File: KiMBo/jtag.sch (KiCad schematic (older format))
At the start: 9 parts, among them U2 OSD3358, Y2 32.768kHz, Y3 24MHz

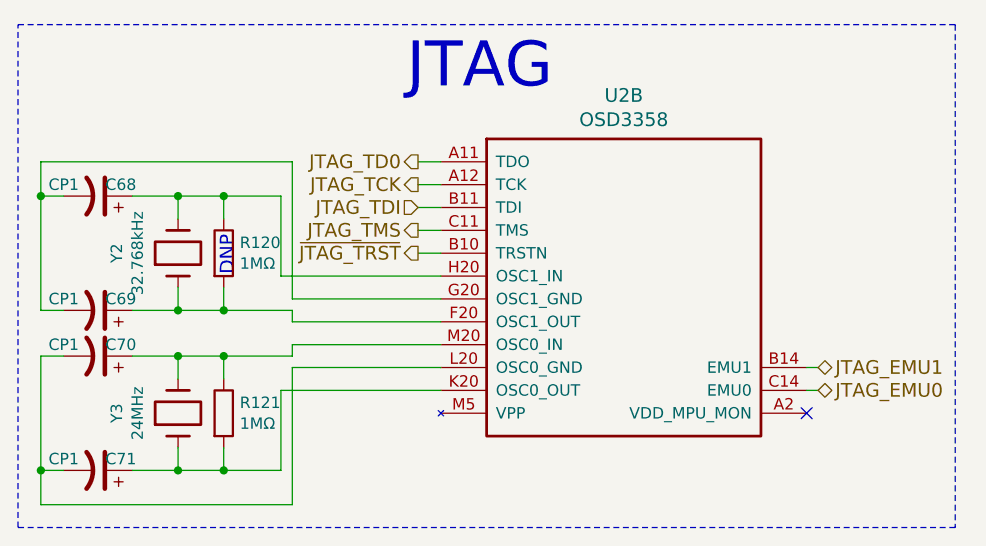
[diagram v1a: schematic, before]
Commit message: Entry of additional component values
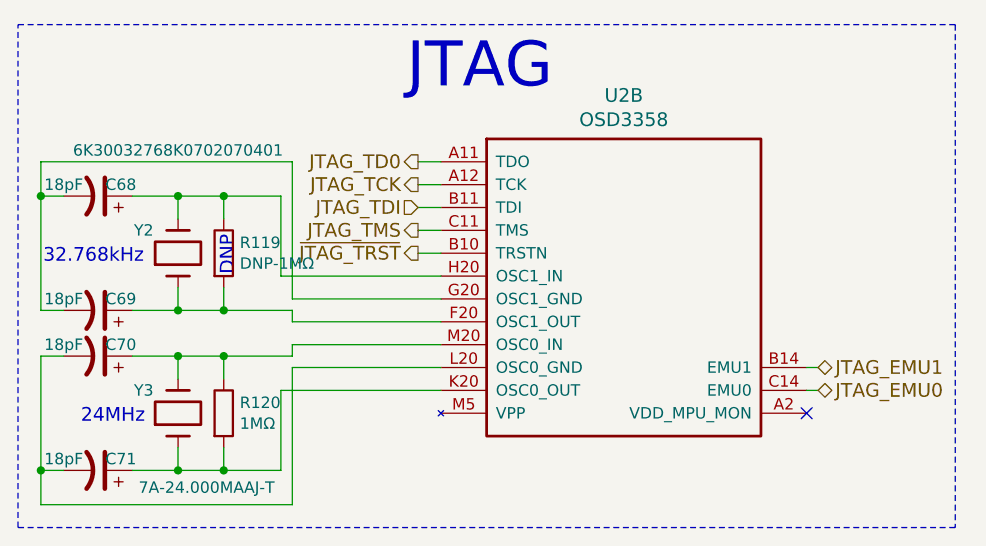
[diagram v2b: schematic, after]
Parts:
- C68, C69, C70, C71: value CP1 -> 18pF
- R119: renamed from R120; value 1MΩ -> DNP-1MΩ
- Y2: value 32.768kHz -> 6K30032768K0702070401
- Y3: value 24MHz -> 7A-24.000MAAJ-T
- renumbered R121 to R120
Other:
- note added: "24MHz"
- note added: "32.768kHz"
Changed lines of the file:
@@
 JTAG
 $Comp
-L R R121
+L R R120
 U 1 1 589C1CFA
 P 4900 4000
-F 0 "R121" H 4970 4046 50  0000 L CNN
+F 0 "R120" H 4970 4046 50  0000 L CNN
 F 1 "1MΩ" H 4970 3955 50  0000 L CNN
 F 2 "" V 4830 4000 50  0001 C CNN
@@
 P 4350 3750
 F 0 "C70" V 4400 3850 50  0000 C CNN
-F 1 "CP1" V 4400 3600 50  0000 C CNN
+F 1 "18pF" V 4400 3600 50  0000 C CNN
 F 2 "" H 4350 3750 50  0001 C CNN
 F 3 "" H 4350 3750 50  0000 C CNN
@@
 P 4350 4250
 F 0 "C71" V 4400 4350 50  0000 C CNN
-F 1 "CP1" V 4400 4100 50  0000 C CNN
+F 1 "18pF" V 4400 4100 50  0000 C CNN
 F 2 "" H 4350 4250 50  0001 C CNN
 F 3 "" H 4350 4250 50  0000 C CNN
@@
 $EndComp
 $Comp
-L R R120
+L R R119
 U 1 1 589C1D0F
 P 4900 3300
-F 0 "R120" H 4970 3346 50  0000 L CNN
-F 1 "1MΩ" H 4970 3255 50  0000 L CNN
+F 0 "R119" H 4970 3346 50  0000 L CNN
+F 1 "DNP-1MΩ" H 4970 3255 50  0000 L CNN
 F 2 "" V 4830 3300 50  0001 C CNN
 F 3 "" H 4900 3300 50  0000 C CNN
@@
 P 4350 3550
 F 0 "C69" V 4400 3650 50  0000 C CNN
-F 1 "CP1" V 4400 3400 50  0000 C CNN
+F 1 "18pF" V 4400 3400 50  0000 C CNN
 F 2 "" H 4350 3550 50  0001 C CNN
 F 3 "" H 4350 3550 50  0000 C CNN
@@
 P 4350 3050
 F 0 "C68" V 4400 3150 50  0000 C CNN
-F 1 "CP1" V 4400 2900 50  0000 C CNN
+F 1 "18pF" V 4400 2900 50  0000 C CNN
 F 2 "" H 4350 3050 50  0001 C CNN
 F 3 "" H 4350 3050 50  0000 C CNN
@@
 U 1 1 589C1D2C
 P 4700 4000
-F 0 "Y3" H 4700 4268 50  0000 C CNN
-F 1 "24MHz" H 4700 4177 50  0000 C CNN
+F 0 "Y3" V 4800 4150 50  0000 C CNN
+F 1 "7A-24.000MAAJ-T" V 4375 3875 50  0000 C CNN
 F 2 "" H 4700 4000 50  0001 C CNN
 F 3 "" H 4700 4000 50  0000 C CNN
@@
 U 1 1 589C1D33
 P 4700 3300
-F 0 "Y2" H 4700 3568 50  0000 C CNN
-F 1 "32.768kHz" H 4700 3477 50  0000 C CNN
+F 0 "Y2" V 4800 3450 50  0000 C CNN
+F 1 "6K30032768K0702070401" V 5150 3300 50  0000 C CNN
 F 2 "" H 4700 3300 50  0001 C CNN
 F 3 "" H 4700 3300 50  0000 C CNN
@@
 Text Notes 4950 3400 1    60   ~ 0
 DNP
+Text Notes 4110 3350 0    60   ~ 0
+32.768kHz
+Text Notes 4275 4050 0    60   ~ 0
+24MHz
 $EndSCHEMATC

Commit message: Replace most electrolytic cap symbols symbols with the standard, non-polarized (ceramic) cap symbol
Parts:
- C68, C69, C70, C71: symbol CP1 -> C
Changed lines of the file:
@@
 $EndComp
 $Comp
-L CP1 C70
+L C C70
 U 1 1 589C1D01
 P 4350 3750
@@
 $EndComp
 $Comp
-L CP1 C71
+L C C71
 U 1 1 589C1D08
 P 4350 4250
@@
 $EndComp
 $Comp
-L CP1 C69
+L C C69
 U 1 1 589C1D16
 P 4350 3550
@@
 $EndComp
 $Comp
-L CP1 C68
+L C C68
 U 1 1 589C1D1D
 P 4350 3050

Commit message: Add equivalent annotations document, associate more footprints
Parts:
- C68, C69, C70, C71: footprint (none) -> Capacitors_SMD:C_0402
- R118: renamed from R119; footprint (none) -> Resistors_SMD:R_0402
- R119: renamed from R120; footprint (none) -> Resistors_SMD:R_0402
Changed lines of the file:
@@
 JTAG
 $Comp
-L R R120
+L R R119
 U 1 1 589C1CFA
 P 4900 4000
-F 0 "R120" H 4970 4046 50  0000 L CNN
+F 0 "R119" H 4970 4046 50  0000 L CNN
 F 1 "1MΩ" H 4970 3955 50  0000 L CNN
-F 2 "" V 4830 4000 50  0001 C CNN
+F 2 "Resistors_SMD:R_0402" V 4830 4000 50  0001 C CNN
 F 3 "" H 4900 4000 50  0000 C CNN
 	1    4900 4000
@@
 F 0 "C70" V 4400 3850 50  0000 C CNN
 F 1 "18pF" V 4400 3600 50  0000 C CNN
-F 2 "" H 4350 3750 50  0001 C CNN
+F 2 "Capacitors_SMD:C_0402" H 4350 3750 50  0001 C CNN
 F 3 "" H 4350 3750 50  0000 C CNN
 	1    4350 3750
@@
 F 0 "C71" V 4400 4350 50  0000 C CNN
 F 1 "18pF" V 4400 4100 50  0000 C CNN
-F 2 "" H 4350 4250 50  0001 C CNN
+F 2 "Capacitors_SMD:C_0402" H 4350 4250 50  0001 C CNN
 F 3 "" H 4350 4250 50  0000 C CNN
 	1    4350 4250
@@
 $EndComp
 $Comp
-L R R119
+L R R118
 U 1 1 589C1D0F
 P 4900 3300
-F 0 "R119" H 4970 3346 50  0000 L CNN
+F 0 "R118" H 4970 3346 50  0000 L CNN
 F 1 "DNP-1MΩ" H 4970 3255 50  0000 L CNN
-F 2 "" V 4830 3300 50  0001 C CNN
+F 2 "Resistors_SMD:R_0402" V 4830 3300 50  0001 C CNN
 F 3 "" H 4900 3300 50  0000 C CNN
 	1    4900 3300
@@
 F 0 "C69" V 4400 3650 50  0000 C CNN
 F 1 "18pF" V 4400 3400 50  0000 C CNN
-F 2 "" H 4350 3550 50  0001 C CNN
+F 2 "Capacitors_SMD:C_0402" H 4350 3550 50  0001 C CNN
 F 3 "" H 4350 3550 50  0000 C CNN
 	1    4350 3550
@@
 F 0 "C68" V 4400 3150 50  0000 C CNN
 F 1 "18pF" V 4400 2900 50  0000 C CNN
-F 2 "" H 4350 3050 50  0001 C CNN
+F 2 "Capacitors_SMD:C_0402" H 4350 3050 50  0001 C CNN
 F 3 "" H 4350 3050 50  0000 C CNN
 	1    4350 3050

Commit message: Leave SPI0 free for a display, reassign pins so SPI1 is available
Fix some typos/errors
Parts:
- renumbered R118 to R120, R119 to R121, U2 to U1
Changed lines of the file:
@@
 P 5850 2900
 AR Path="/581AEC7B/589C1CF2" Ref="U?"  Part="2"
-AR Path="/589C1616/589C1CF2" Ref="U2"  Part="2"
-F 0 "U2" H 6650 3190 60  0000 C CNN
+AR Path="/589C1616/589C1CF2" Ref="U1"  Part="2"
+F 0 "U1" H 6650 3190 60  0000 C CNN
 F 1 "OSD3358" H 6650 3084 60  0000 C CNN
 F 2 "" H 5850 2900 60  0001 C CNN
@@
 JTAG
 $Comp
-L R R119
+L R R121
 U 1 1 589C1CFA
 P 4900 4000
-F 0 "R119" H 4970 4046 50  0000 L CNN
+F 0 "R121" H 4970 4046 50  0000 L CNN
 F 1 "1MΩ" H 4970 3955 50  0000 L CNN
 F 2 "Resistors_SMD:R_0402" V 4830 4000 50  0001 C CNN
@@
 $EndComp
 $Comp
-L R R118
+L R R120
 U 1 1 589C1D0F
 P 4900 3300
-F 0 "R118" H 4970 3346 50  0000 L CNN
+F 0 "R120" H 4970 3346 50  0000 L CNN
 F 1 "DNP-1MΩ" H 4970 3255 50  0000 L CNN
 F 2 "Resistors_SMD:R_0402" V 4830 3300 50  0001 C CNN

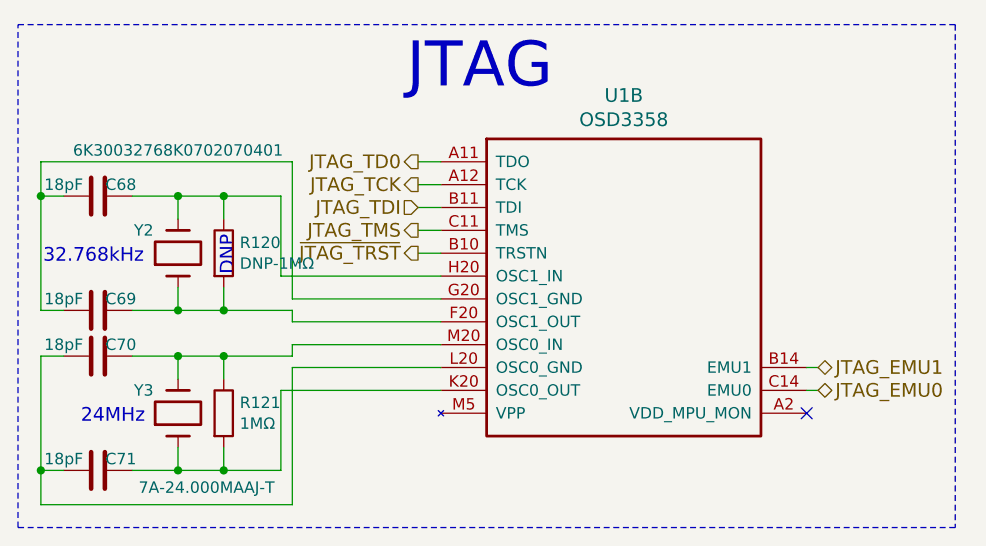
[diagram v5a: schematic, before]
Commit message: Use fixed 5V LM2592HV Buck, include SPI0 header for LCD
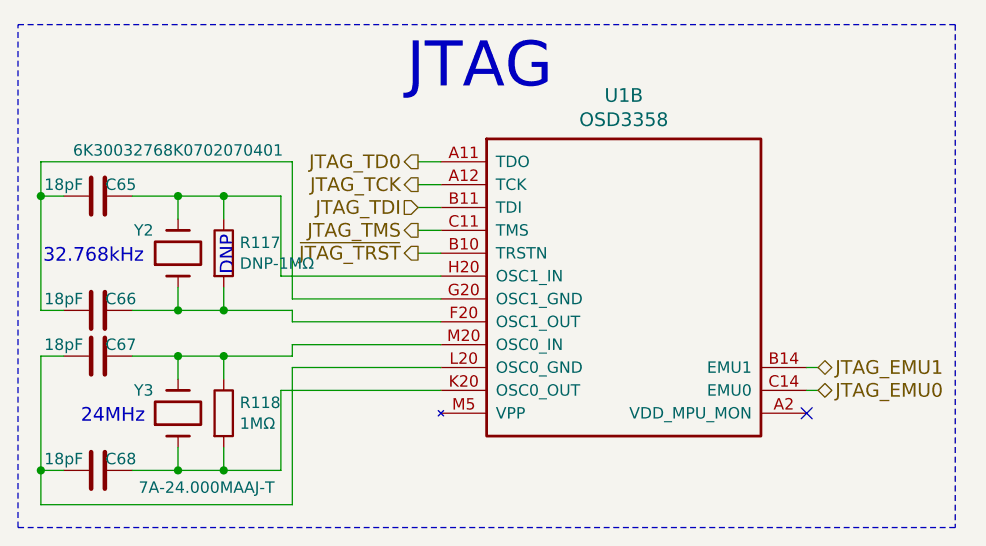
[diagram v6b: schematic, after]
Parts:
- renumbered C68 to C65, C69 to C66, C70 to C67, C71 to C68, R120 to R117, R121 to R118
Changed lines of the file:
@@
 JTAG
 $Comp
-L R R121
+L R R118
 U 1 1 589C1CFA
 P 4900 4000
-F 0 "R121" H 4970 4046 50  0000 L CNN
+F 0 "R118" H 4970 4046 50  0000 L CNN
 F 1 "1MΩ" H 4970 3955 50  0000 L CNN
 F 2 "Resistors_SMD:R_0402" V 4830 4000 50  0001 C CNN
@@
 $EndComp
 $Comp
-L C C70
+L C C67
 U 1 1 589C1D01
 P 4350 3750
-F 0 "C70" V 4400 3850 50  0000 C CNN
+F 0 "C67" V 4400 3850 50  0000 C CNN
 F 1 "18pF" V 4400 3600 50  0000 C CNN
 F 2 "Capacitors_SMD:C_0402" H 4350 3750 50  0001 C CNN
@@
 $EndComp
 $Comp
-L C C71
+L C C68
 U 1 1 589C1D08
 P 4350 4250
-F 0 "C71" V 4400 4350 50  0000 C CNN
+F 0 "C68" V 4400 4350 50  0000 C CNN
 F 1 "18pF" V 4400 4100 50  0000 C CNN
 F 2 "Capacitors_SMD:C_0402" H 4350 4250 50  0001 C CNN
@@
 $EndComp
 $Comp
-L R R120
+L R R117
 U 1 1 589C1D0F
 P 4900 3300
-F 0 "R120" H 4970 3346 50  0000 L CNN
+F 0 "R117" H 4970 3346 50  0000 L CNN
 F 1 "DNP-1MΩ" H 4970 3255 50  0000 L CNN
 F 2 "Resistors_SMD:R_0402" V 4830 3300 50  0001 C CNN
@@
 $EndComp
 $Comp
-L C C69
+L C C66
 U 1 1 589C1D16
 P 4350 3550
-F 0 "C69" V 4400 3650 50  0000 C CNN
+F 0 "C66" V 4400 3650 50  0000 C CNN
 F 1 "18pF" V 4400 3400 50  0000 C CNN
 F 2 "Capacitors_SMD:C_0402" H 4350 3550 50  0001 C CNN
@@
 $EndComp
 $Comp
-L C C68
+L C C65
 U 1 1 589C1D1D
 P 4350 3050
-F 0 "C68" V 4400 3150 50  0000 C CNN
+F 0 "C65" V 4400 3150 50  0000 C CNN
 F 1 "18pF" V 4400 2900 50  0000 C CNN
 F 2 "Capacitors_SMD:C_0402" H 4350 3050 50  0001 C CNN

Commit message: Assocate more footprints
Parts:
- C65, C66, C67, C68: footprint Capacitors_SMD:C_0402 -> Capacitors_SMD:C_0603
- R117, R118: footprint Resistors_SMD:R_0402 -> Resistors_SMD:R_0603
- U1: footprint (none) -> KiMBo:BGA-400-1-27mm
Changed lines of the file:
@@
 F 0 "U1" H 6650 3190 60  0000 C CNN
 F 1 "OSD3358" H 6650 3084 60  0000 C CNN
-F 2 "" H 5850 2900 60  0001 C CNN
+F 2 "KiMBo:BGA-400-1-27mm" H 5850 2900 60  0001 C CNN
 F 3 "" H 5850 2900 60  0001 C CNN
 	2    5850 2900
@@
 F 0 "R118" H 4970 4046 50  0000 L CNN
 F 1 "1MΩ" H 4970 3955 50  0000 L CNN
-F 2 "Resistors_SMD:R_0402" V 4830 4000 50  0001 C CNN
+F 2 "Resistors_SMD:R_0603" V 4830 4000 50  0001 C CNN
 F 3 "" H 4900 4000 50  0000 C CNN
 	1    4900 4000
@@
 F 0 "C67" V 4400 3850 50  0000 C CNN
 F 1 "18pF" V 4400 3600 50  0000 C CNN
-F 2 "Capacitors_SMD:C_0402" H 4350 3750 50  0001 C CNN
+F 2 "Capacitors_SMD:C_0603" H 4350 3750 50  0001 C CNN
 F 3 "" H 4350 3750 50  0000 C CNN
 	1    4350 3750
@@
 F 0 "C68" V 4400 4350 50  0000 C CNN
 F 1 "18pF" V 4400 4100 50  0000 C CNN
-F 2 "Capacitors_SMD:C_0402" H 4350 4250 50  0001 C CNN
+F 2 "Capacitors_SMD:C_0603" H 4350 4250 50  0001 C CNN
 F 3 "" H 4350 4250 50  0000 C CNN
 	1    4350 4250
@@
 F 0 "R117" H 4970 3346 50  0000 L CNN
 F 1 "DNP-1MΩ" H 4970 3255 50  0000 L CNN
-F 2 "Resistors_SMD:R_0402" V 4830 3300 50  0001 C CNN
+F 2 "Resistors_SMD:R_0603" V 4830 3300 50  0001 C CNN
 F 3 "" H 4900 3300 50  0000 C CNN
 	1    4900 3300
@@
 F 0 "C66" V 4400 3650 50  0000 C CNN
 F 1 "18pF" V 4400 3400 50  0000 C CNN
-F 2 "Capacitors_SMD:C_0402" H 4350 3550 50  0001 C CNN
+F 2 "Capacitors_SMD:C_0603" H 4350 3550 50  0001 C CNN
 F 3 "" H 4350 3550 50  0000 C CNN
 	1    4350 3550
@@
 F 0 "C65" V 4400 3150 50  0000 C CNN
 F 1 "18pF" V 4400 2900 50  0000 C CNN
-F 2 "Capacitors_SMD:C_0402" H 4350 3050 50  0001 C CNN
+F 2 "Capacitors_SMD:C_0603" H 4350 3050 50  0001 C CNN
 F 3 "" H 4350 3050 50  0000 C CNN
 	1    4350 3050

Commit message: More footprint association
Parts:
- R117: footprint Resistors_SMD:R_0603 -> (none)
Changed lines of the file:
@@
 F 0 "R117" H 4970 3346 50  0000 L CNN
 F 1 "DNP-1MΩ" H 4970 3255 50  0000 L CNN
-F 2 "Resistors_SMD:R_0603" V 4830 3300 50  0001 C CNN
+F 2 "" V 4830 3300 50  0001 C CNN
 F 3 "" H 4900 3300 50  0000 C CNN
 	1    4900 3300
